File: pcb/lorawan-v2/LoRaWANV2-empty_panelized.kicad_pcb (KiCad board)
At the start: 2 copper layers, 99.9 x 99.9 mm, 0 parts

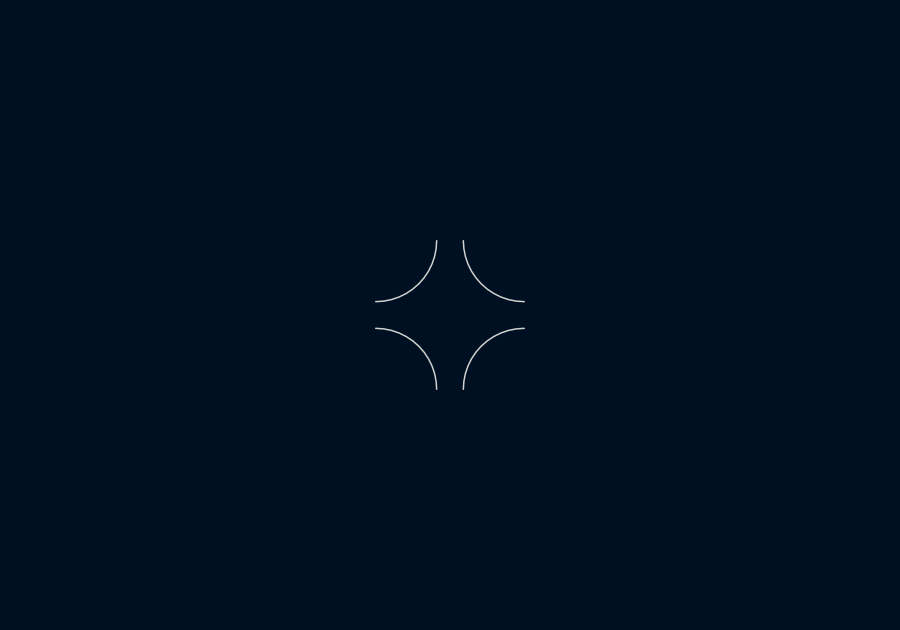
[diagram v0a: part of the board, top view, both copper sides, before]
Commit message: new LoRaWAN V2.1 sent to manufacturing
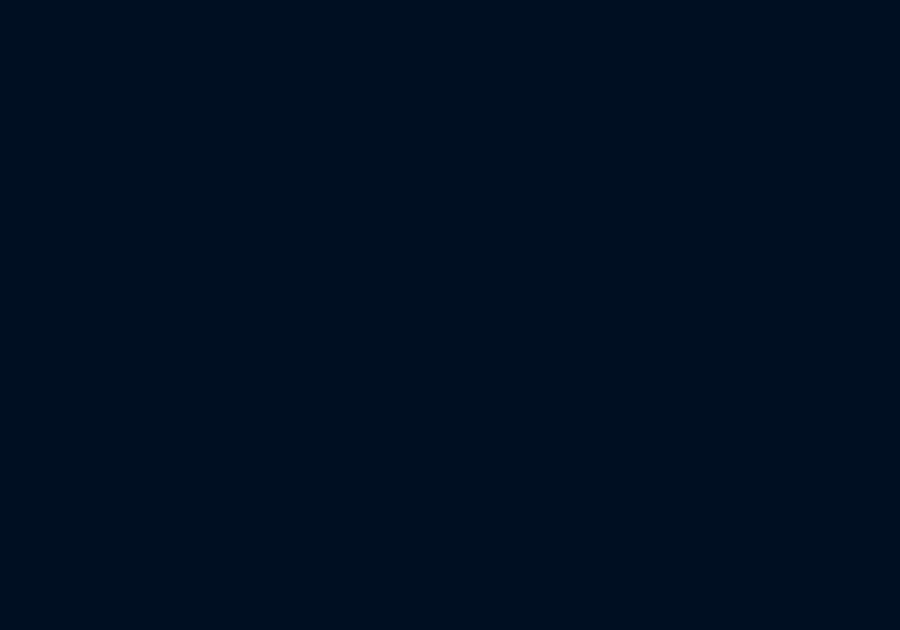
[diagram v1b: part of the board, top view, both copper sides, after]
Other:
- outline, holes or cut-outs redrawn
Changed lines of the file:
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@@
   (general
     (thickness 1.6)
-    (drawings 60)
+    (drawings 56)
     (tracks 0)
     (zones 0)
@@
   )
   (gr_arc (start 40.132 136.017) (end 40.132 138.049) (angle 90) (layer Edge.Cuts) (width 0.05))
-  (gr_arc (start 90.551 90.551) (end 90.551 88.519) (angle -90) (layer Edge.Cuts) (width 0.05))
-  (gr_arc (start 85.598 90.551) (end 85.598 88.519) (angle 90) (layer Edge.Cuts) (width 0.05))
   (gr_line (start 87.63 40.132) (end 88.519 40.132) (layer Edge.Cuts) (width 0.05))
   (gr_line (start 136.017 87.63) (end 136.017 88.519) (layer Edge.Cuts) (width 0.05))
@@
   (gr_line (start 40.132 138.049) (end 85.598 138.049) (layer Edge.Cuts) (width 0.05))
   (gr_arc (start 40.132 85.598) (end 38.1 85.598) (angle -90) (layer Edge.Cuts) (width 0.05))
-  (gr_arc (start 85.598 85.598) (end 85.598 87.63) (angle -90) (layer Edge.Cuts) (width 0.05))
   (gr_arc (start 85.598 40.132) (end 87.63 40.132) (angle -90) (layer Edge.Cuts) (width 0.05))
   (gr_arc (start 40.132 40.132) (end 40.132 38.1) (angle -90) (layer Edge.Cuts) (width 0.05))
@@
   (gr_line (start 40.132 38.1) (end 85.598 38.1) (layer Edge.Cuts) (width 0.05))
   (gr_arc (start 136.017 85.598) (end 138.049 85.598) (angle 90) (layer Edge.Cuts) (width 0.05))
-  (gr_arc (start 90.551 85.598) (end 90.551 87.63) (angle 90) (layer Edge.Cuts) (width 0.05))
   (gr_arc (start 90.551 40.132) (end 88.519 40.132) (angle 90) (layer Edge.Cuts) (width 0.05))
   (gr_arc (start 136.017 40.132) (end 136.017 38.1) (angle 90) (layer Edge.Cuts) (width 0.05))
